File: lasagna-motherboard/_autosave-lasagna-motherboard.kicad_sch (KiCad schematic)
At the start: 13 parts

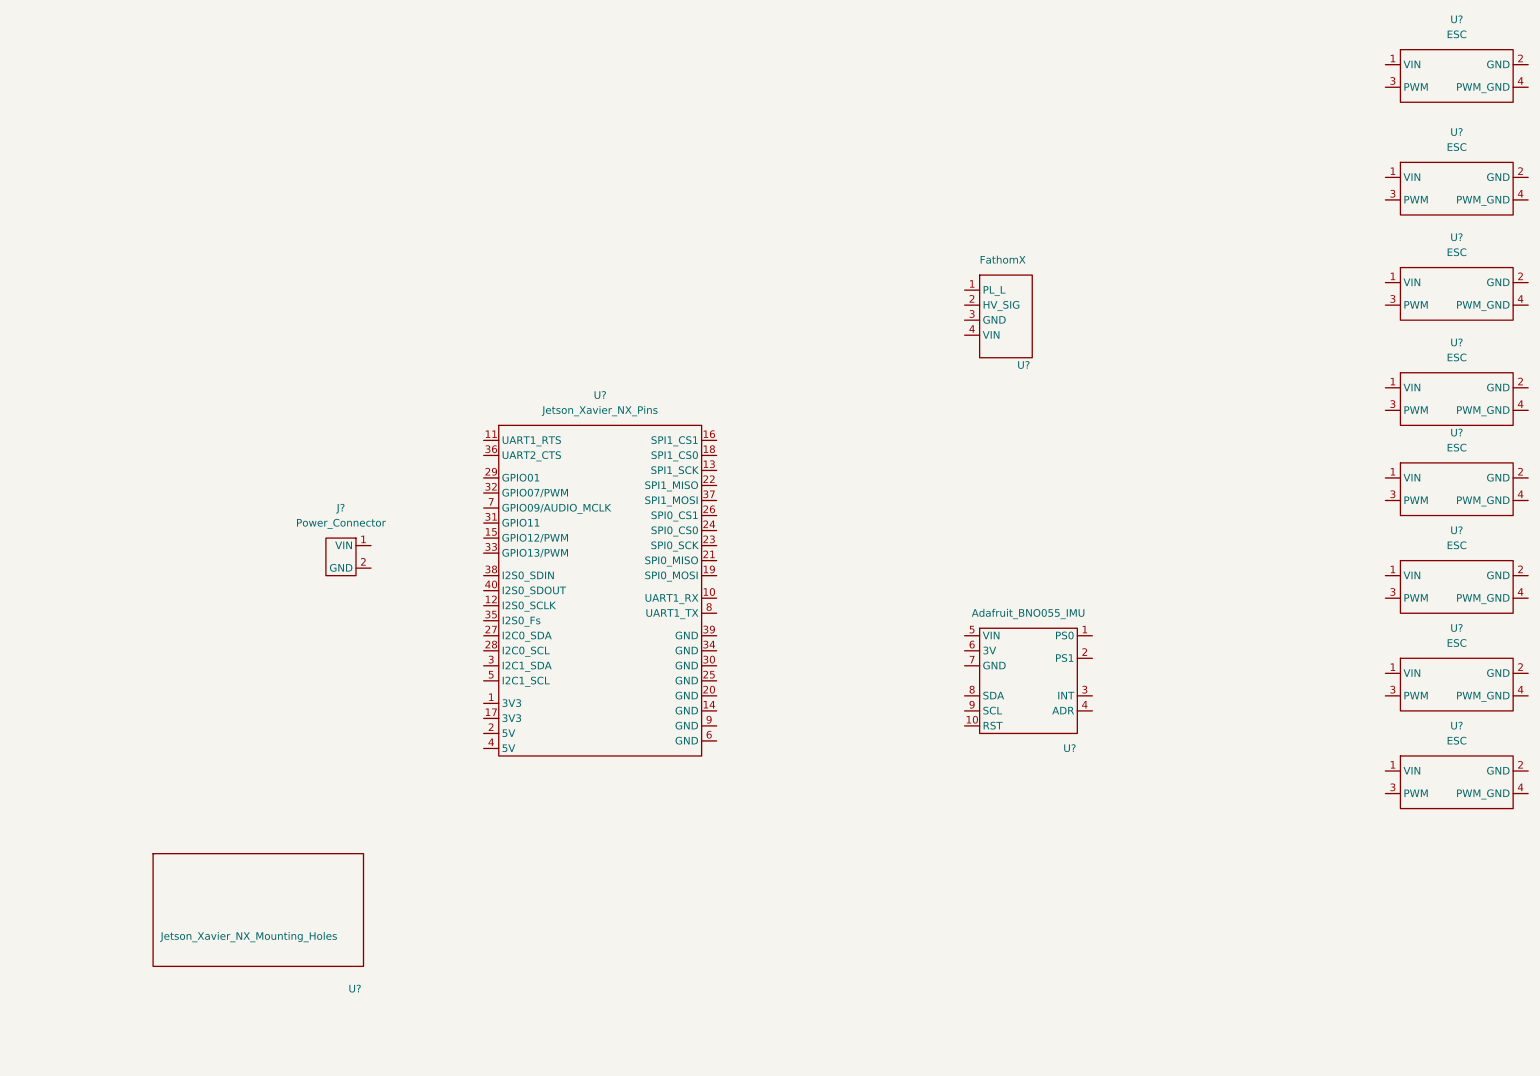
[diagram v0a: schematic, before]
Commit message: added the servo connectors
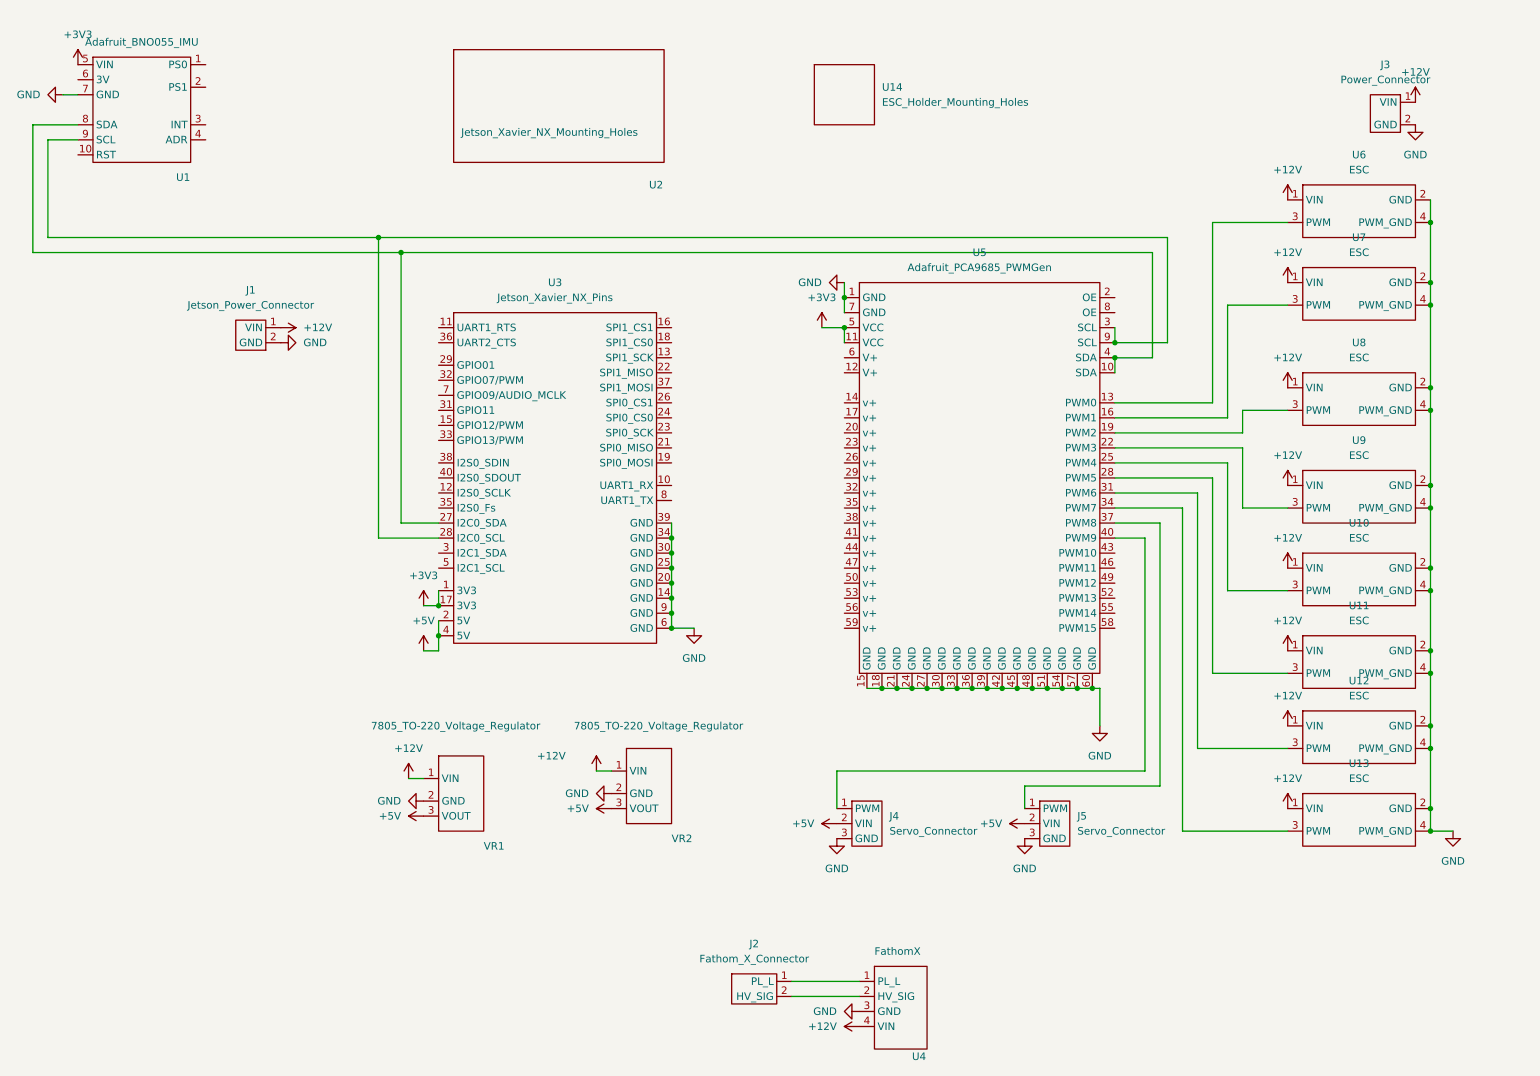
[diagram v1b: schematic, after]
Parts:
- removed U? (x7): ESC, symbol lasagna-motherboard:ESC
- added J1: Jetson_Power_Connector, lasagna-motherboard:Jetson Power Connector, symbol lasagna-motherboard:Jetson_Power_Connector
- added J2: Fathom_X_Connector, lasagna-motherboard:FathomX_Connector, symbol lasagna-motherboard:Fathom_X_Connector
- added J4, J5: Servo_Connector, lasagna-motherboard:Servo PWM Connector, symbol lasagna-motherboard:Servo_Connector
- added U10, U11, U12, U13, U7, U8, U9: ESC, lasagna-motherboard:ESC, symbol lasagna-motherboard:ESC
- added U14: ESC_Holder_Mounting_Holes, lasagna-motherboard:ESC Holder mounting Holes, symbol lasagna-motherboard:ESC_Holder_Mounting_Holes
- added U5: Adafruit_PCA9685_PWMGen, lasagna-motherboard:Adafruit_PCA9685_PWMGen, symbol lasagna-motherboard:Adafruit_PCA9685_PWMGen
- added VR1, VR2: 7805_TO-220_Voltage_Regulator, lasagna-motherboard:Voltage Regulator TO255, symbol lasagna-motherboard:7805_TO-220_Voltage_Regulator
- J3: renamed from J?; footprint (none) -> lasagna-motherboard:Power_Connector
- U1: renamed from U?; footprint (none) -> lasagna-motherboard:Adafruit_BNO055_IMU
- U2: renamed from U?; footprint (none) -> lasagna-motherboard:Jetson_Xavier_NX_Mounting_Holes
- U3: renamed from U?; footprint (none) -> lasagna-motherboard:Jetson_Xavier_NX_2X20_Pin_Header
- U4: renamed from U?; footprint (none) -> lasagna-motherboard:FathomX
- U6: renamed from U?; footprint (none) -> lasagna-motherboard:ESC
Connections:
- net +3V3: now reaches U3.1 (3V3)
- net +3V3: now also U1.5 (VIN), U3.17 (3V3), U5.11 (VCC), U5.5 (VCC)
- net GND: now reaches U3.14 (GND)
- net GND: now also J3.2 (GND), U1.7 (GND), U3.20 (GND), U3.25 (GND), U3.30 (GND), U3.34 (GND), U3.39 (GND), U3.6 (GND), U3.9 (GND), U4.3 (GND), U6.2 (GND), U6.4 (PWM_GND), J1.2 (GND), J4.3 (GND), J5.3 (GND), U10.2 (GND), U10.4 (PWM_GND), U11.2 (GND), U11.4 (PWM_GND), U12.2 (GND), U12.4 (PWM_GND), U13.2 (GND), U13.4 (PWM_GND), U5.1 (GND), U5.15 (GND), U5.18 (GND), U5.21 (GND), U5.24 (GND), U5.27 (GND), U5.30 (GND), U5.33 (GND), U5.36 (GND), U5.39 (GND), U5.42 (GND), U5.45 (GND), U5.48 (GND), U5.51 (GND), U5.54 (GND), U5.57 (GND), U5.60 (GND), U5.7 (GND), U7.2 (GND), U7.4 (PWM_GND), U8.2 (GND), U8.4 (PWM_GND), U9.2 (GND), U9.4 (PWM_GND), VR1.2 (GND), VR2.2 (GND)
- net +5V: now reaches U3.2 (5V)
- net +5V: now also U3.4 (5V), J4.2 (VIN), J5.2 (VIN), VR1.3 (VOUT), VR2.3 (VOUT)
- net at U3.27 (I2C0_SDA): now also U1.8 (SDA), U5.10 (SDA), U5.4 (SDA)
- net at U3.28 (I2C0_SCL): now also U1.9 (SCL), U5.3 (SCL), U5.9 (SCL)
- net +12V: now reaches J3.1 (VIN)
- net +12V: now also U4.4 (VIN), U6.1 (VIN), J1.1 (VIN), U10.1 (VIN), U11.1 (VIN), U12.1 (VIN), U13.1 (VIN), U7.1 (VIN), U8.1 (VIN), U9.1 (VIN), VR1.1 (VIN), VR2.1 (VIN)
- net at U4.1 (PL_L): now also J2.1 (PL_L)
- net at U4.2 (HV_SIG): now also J2.2 (HV_SIG)
- net at U6.3 (PWM): now also U5.13 (PWM0)
- new net: U10.3 (PWM), U5.25 (PWM4)
- new net: U5.19 (PWM2), U8.3 (PWM)
- new net: U12.3 (PWM), U5.31 (PWM6)
- new net: U13.3 (PWM), U5.34 (PWM7)
- new net: U5.22 (PWM3), U9.3 (PWM)
- new net: U5.16 (PWM1), U7.3 (PWM)
- new net: U11.3 (PWM), U5.28 (PWM5)
- new net: J5.1 (PWM), U5.37 (PWM8)
- new net: J4.1 (PWM), U5.40 (PWM9)
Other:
- moved on the sheet: J3, U1, U2, U3, U4, U6
